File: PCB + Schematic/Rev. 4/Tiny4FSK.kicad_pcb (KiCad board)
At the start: 4 copper layers, 25.2 x 64 mm, 71 parts, among them IC1 SI4063, J1 SWD, J2 GPIO, J4 USB, J5 I2C, J6 Power, J7 SPI, SW1 RST, SW2 BATT PWR, U1 BME280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

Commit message: Finish USB breakout
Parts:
- BT1: value AAA -> Battery_Cell; footprint BatteryExtended:BAT_BK-82 -> BatteryExtended:BAT_53; moved to B.Cu
- C12: value 10uF -> 100 nF
- C13, C7: value 100nF -> 10 uF
- C9: value 100nF -> 100 nF
- R11: value 900k -> 180k
- R12: value 5M -> 1M
- moved BT1 42.7 mm to (150.2, 74.9), turned to -90 degrees
- moved R12 4.15 mm to (151.5, 72.0), turned to 0 degrees
- moved AE1 4.01 mm to (152.4, 42.0)
- moved R11 3.61 mm to (155.5, 72.0), turned to 0 degrees
- moved C23 1.51 mm to (150.5, 96.8)
- moved XTAL1 0.79 mm to (146.0, 94.0)
- moved IC1 0.50 mm to (152.5, 92.0)
- moved C27 0.19 mm to (154.3, 100.2)
- moved AE2 0.18 mm to (153.9, 97.8)
- moved C22 0.11 mm to (154.4, 95.2)
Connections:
- C17 pad 1: BOOST -> +3.3V
- C21 pad 1: BOOST -> +3.3V
- R12 pad 1: BOOST -> +3.3V
- U6 pad 2: BOOST -> +3.3V
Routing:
- net Earth: track 19.6 -> 48.9 mm, vias 16 -> 35
- net BOOST: track 12.7 -> 0.00 mm, vias 2 -> 0
- net +3.3V: track 67.5 -> 77.8 mm, vias 14 -> 18
- net +BATT: track 19.4 -> 28.4 mm, vias 1 -> 2
- net MISO: track 32.7 -> 41.7 mm
- net RXD: track 37.8 -> 45.9 mm
- net TXD: track 35.8 -> 43.1 mm
- net SCL: track 57.4 -> 62.4 mm
- net ANT_GPS: track 4.35 -> 8.33 mm
- net GPIO1: track 6.56 -> 10.3 mm
- net RF_SS: track 12.7 -> 15.8 mm
- net A1: track 24.8 -> 27.7 mm
- net SDA: track 57.7 -> 60.5 mm
- net ERROR: track 28.9 -> 31.5 mm
- net MOSI: track 30.4 -> 32.8 mm
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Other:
- board size 25.2 x 64 mm -> 25.2 x 67.8 mm
- board text added: "Please leave antenna unobstructed!"

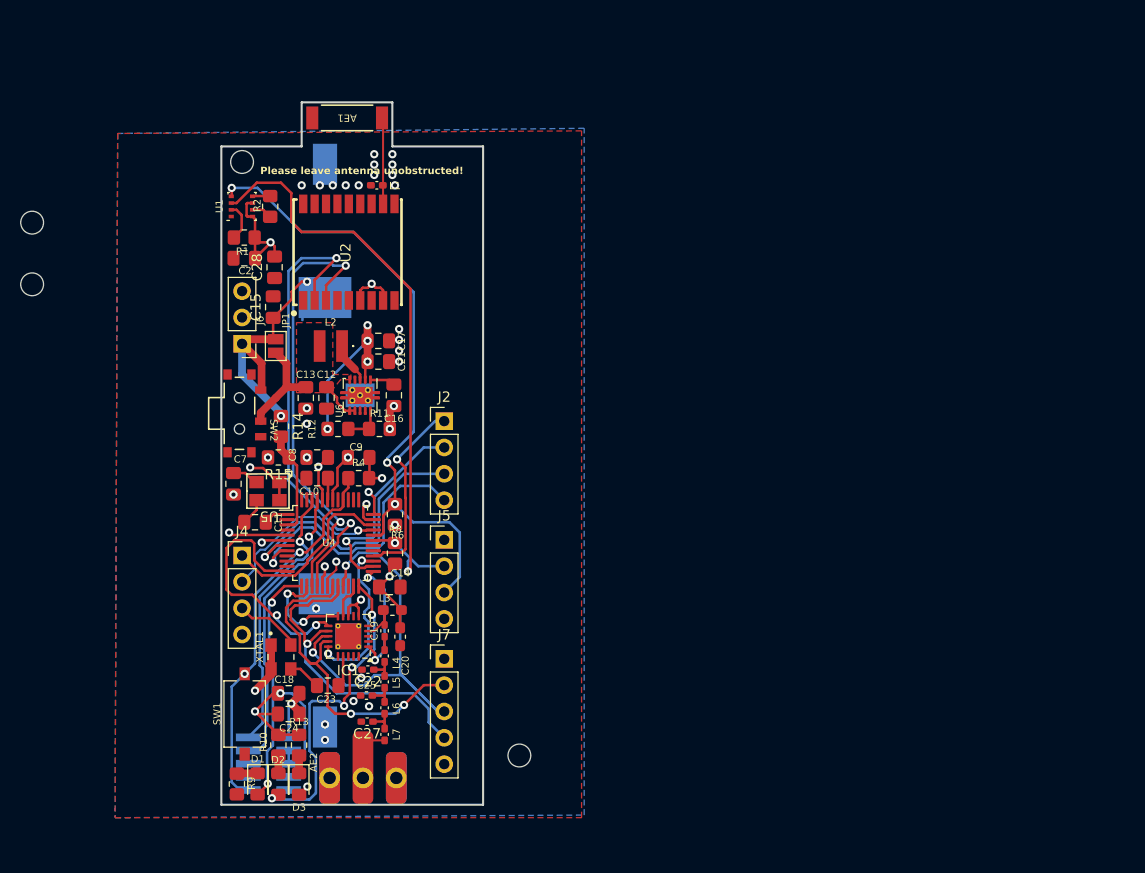
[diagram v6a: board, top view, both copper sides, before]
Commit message: Make DRC happy
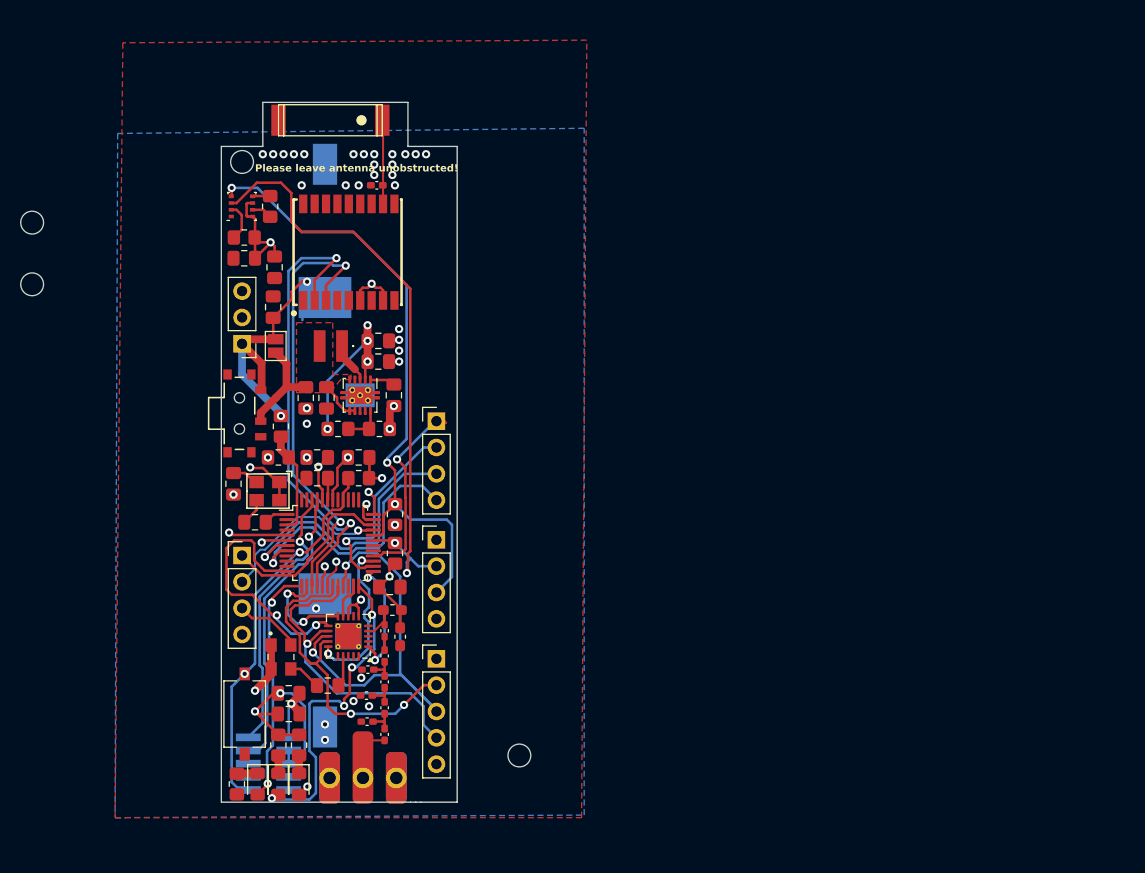
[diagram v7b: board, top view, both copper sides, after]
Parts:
- AE1: footprint RF_Antenna_Extended:ANT_1575AT_JOT -> RF_Antenna_Extended:GPS1003
- moved AE1 4.87 mm to (157.2, 42.1), turned to -90 degrees
- moved J2 0.75 mm to (161.0, 71.2)
- moved J5 0.75 mm to (161.0, 82.7)
- moved J7 0.75 mm to (161.0, 94.2)
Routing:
- net SCL: track 62.4 -> 61.6 mm
- net MOSI: track 32.8 -> 32.1 mm
- net D13: track 20.0 -> 19.2 mm
- net A2: track 27.1 -> 26.4 mm
- net A1: track 27.7 -> 27.0 mm
- net Earth: vias 35 -> 43
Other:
- board size 25.2 x 67.8 mm -> 22.8 x 67.5 mm

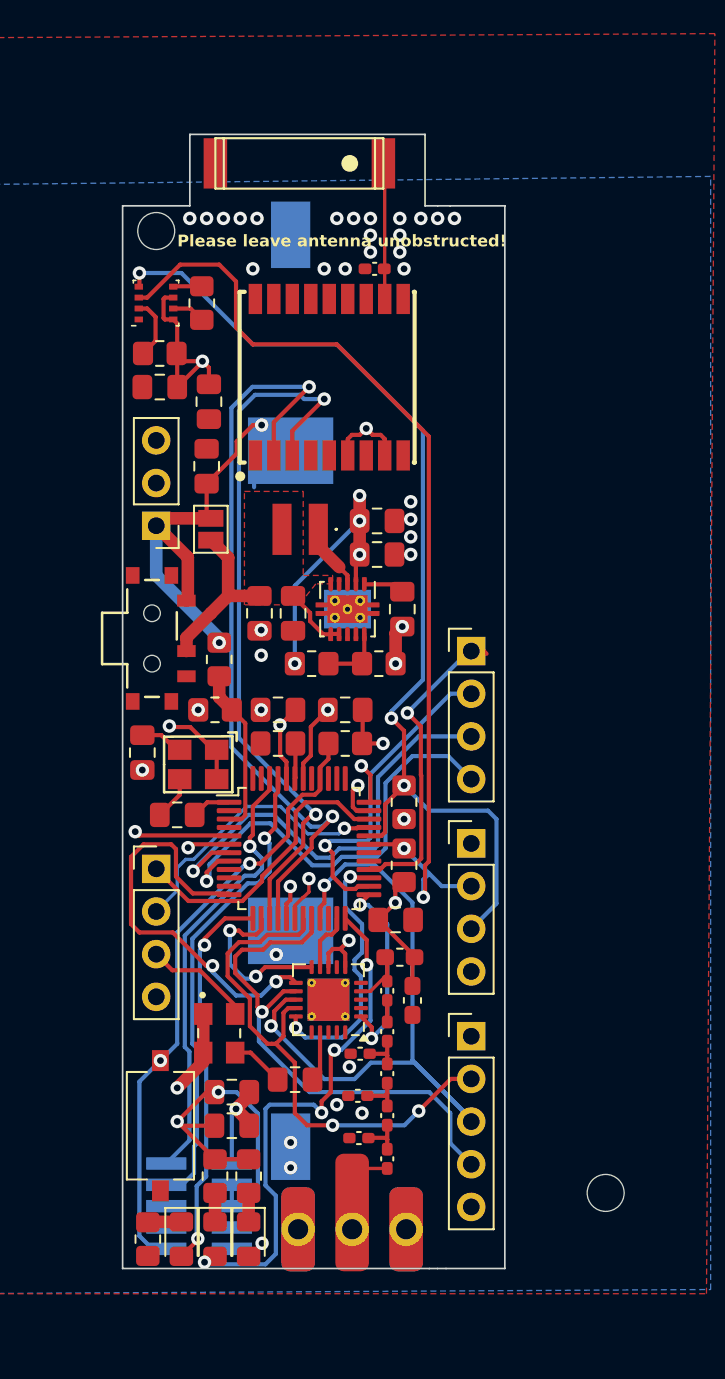
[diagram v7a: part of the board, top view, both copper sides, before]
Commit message: JLCPCB part numbering, PCB updates
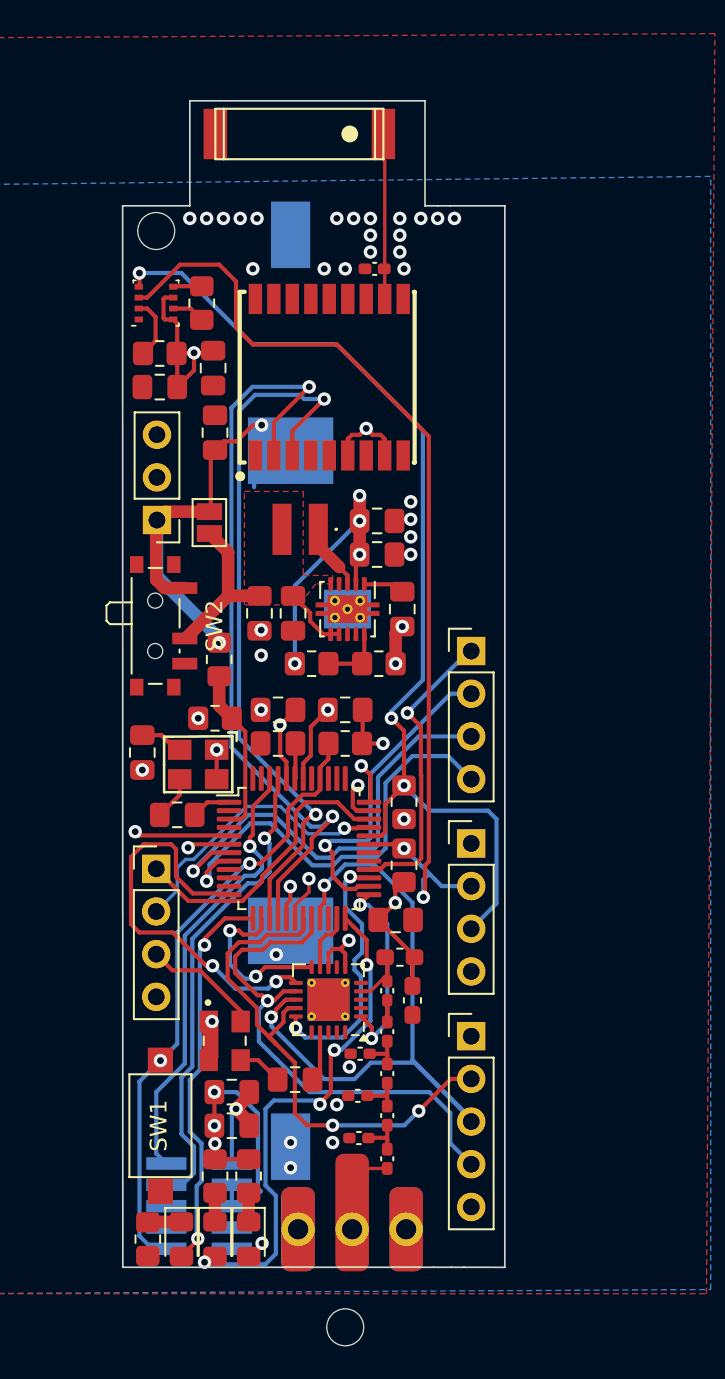
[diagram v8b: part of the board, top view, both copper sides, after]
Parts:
- SW1: footprint Button_Switch_SMD:SW_Tactile_SPST_NO_Straight_CK_PTS636Sx25SMTRLFS -> Button_Switch_SMD:SW_SPST_CK_RS282G05A3
- SW2: footprint SlideSwitch:WS-SLSU_6p7x2p7_WRE -> Button_Switch_SMD:SW_SPDT_PCM12
- moved H4 17.4 mm to (153.5, 111.5)
- moved C15 2.06 mm to (145.8, 58.2)
- moved C28 2.02 mm to (145.6, 54.4)
- moved AE1 1.75 mm to (157.2, 40.4)
- moved SW2 0.91 mm to (142.5, 69.8), turned to -90 degrees
- moved XTAL1 0.55 mm to (146.3, 94.4)
- moved R15 0.50 mm to (145.8, 75.2)
- moved JP1 0.41 mm to (145.4, 63.6)
- moved J6 0.34 mm to (142.3, 63.5)
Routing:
- net Earth: track 48.9 -> 44.5 mm, vias 43 -> 44
- net +3.3V: track 77.8 -> 74.4 mm
- net D12: track 18.6 -> 17.6 mm
- net RF_RST: track 24.7 -> 24.1 mm
- net ERROR: track 31.5 -> 30.9 mm
- net RF_XO: track 3.19 -> 2.68 mm
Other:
- board size 22.8 x 67.5 mm -> 22.8 x 69.4 mm
- board text removed: "Please leave antenna unobstructed!"
